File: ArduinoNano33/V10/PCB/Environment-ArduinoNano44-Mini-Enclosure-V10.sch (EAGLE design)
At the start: 53 parts, among them IC1 BME680, Q1 310mA/60V/1.6Ω, Q2 310mA/60V/1.6Ω

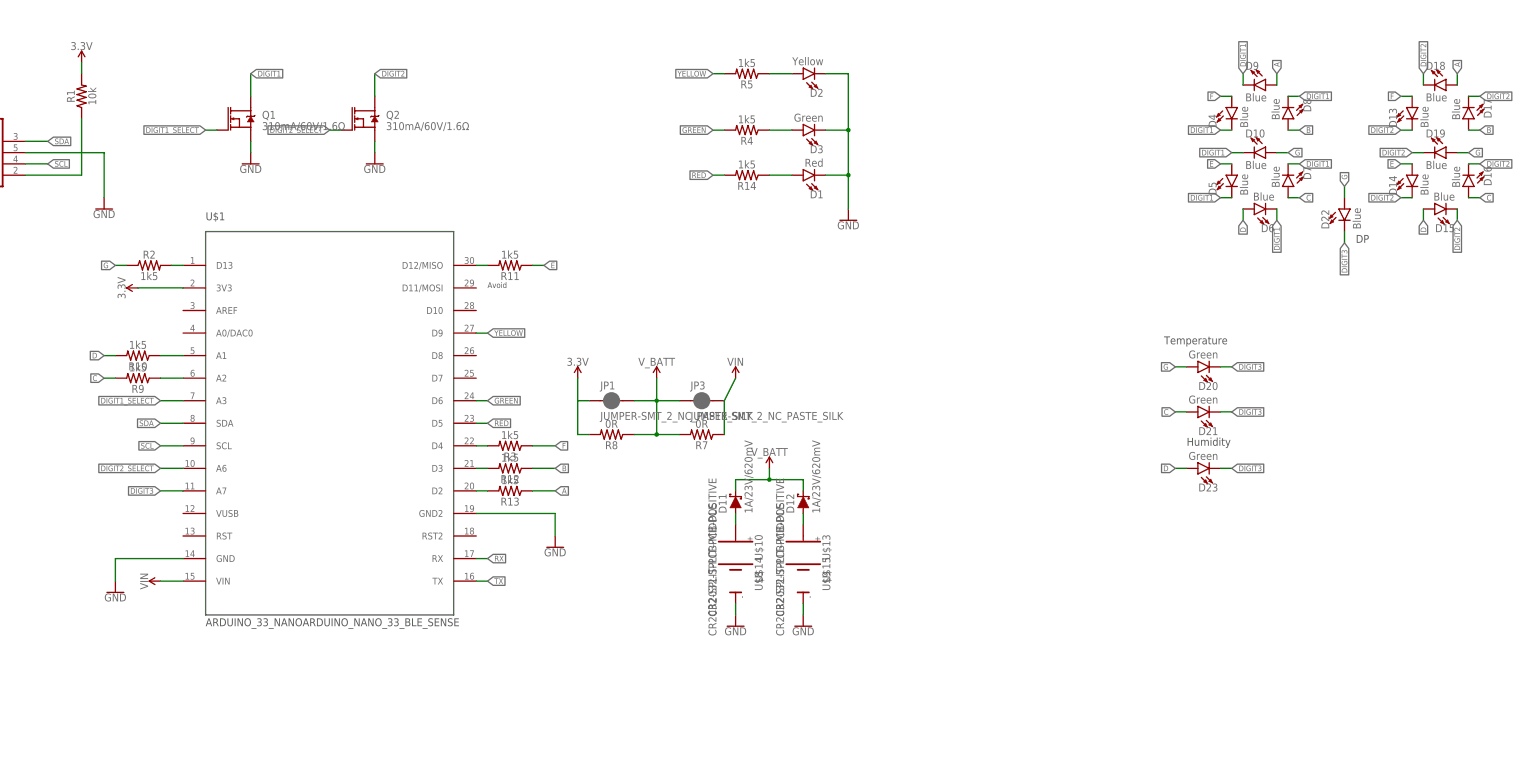
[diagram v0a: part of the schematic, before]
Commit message: added 7 segment display from LEDs.
Added batteries as internal layers
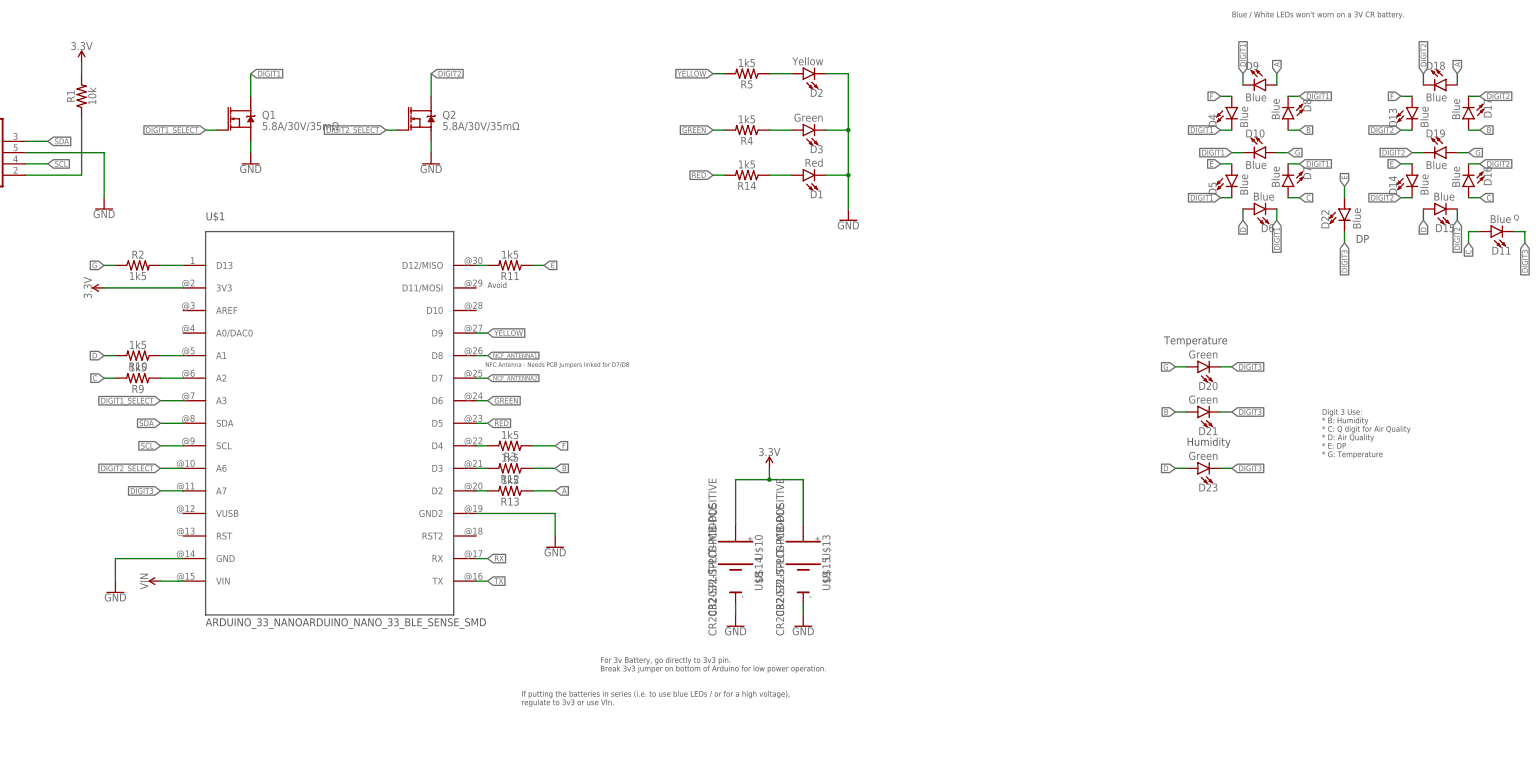
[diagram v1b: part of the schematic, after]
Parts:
- removed D12: 1A/23V/620mV, SparkFun-DiscreteSemi:DIODE-SCHOTTKY-BAT20J
- removed JP1, JP3: JUMPER-SMT_2_NC_PASTE_SILK, SparkFun-Jumpers:JUMPER-SMT_2_NC_PASTE_SILK
- removed R7, R8: 0R, SparkFun-Resistors:RESISTOR0805
- D11: value 1A/23V/620mV -> Blue; device SparkFun-DiscreteSemi:DIODE-SCHOTTKY-BAT20J -> ThingySticks:LED1206
- Q1, Q2: value 310mA/60V/1.6Ω -> 5.8A/30V/35mΩ; device SparkFun-DiscreteSemi:MOSFET-NCH-2N7002PW -> SparkFun-DiscreteSemi:MOSFET-NCH-AO3404A
- U$1: value ARDUINO_33_NANOARDUINO_NANO_33_BLE_SENSE -> ARDUINO_33_NANOARDUINO_NANO_33_BLE_SENSE_SMD; device ThingySticks:ARDUINO_33_NANOARDUINO_NANO_33_BLE_SENSE -> ThingySticks:ARDUINO_33_NANOARDUINO_NANO_33_BLE_SENSE_SMD
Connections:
- removed net N$5: D11.A, U$10.+
- removed net N$6: D12.A, U$13.+
- removed net V_BATT: D11.C, D12.C, JP1.2, JP3.1, R7.2, R8.1
- new net NCF_ANTENNA1: U$1.D8
- new net NCF_ANTENNA2: U$1.D7
- net 3.3V: now also U$10.+, U$13.+; no longer JP1.1, R8.2
- net B: now also D21.A
- net C: now also D11.A; no longer D21.A
- net DIGIT3: now also D11.C
- net E: now also D22.A
- net G: no longer D22.A
- net VIN: no longer JP3.2, R7.1
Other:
- note added: "Blue / White LEDs won't worn on a 3V CR battery."
- note added: "Digit 3 Use: * B: Humidity * C: Q digit for Air Quality * D: Air Quality * E: DP * G: Temperature"
- note added: "For 3v Battery, go directly to 3v3 pin. Break 3v3 jumper on bottom of Arduino for low power operation."
- note added: "If putting the batteries in series (i.e. to use blue LEDs / or for a high voltage), regulate to 3v3 or use VIn."
- note added: "NFC Antenna - Needs PCB Jumpers linked for D7/D8"
- note added: "Q"
- moved on the sheet: Q2, R2

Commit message: Split out personal environmental sensor boards into individual Eagle files.
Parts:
- removed JP2: USB-NEW-MICROB, Tinamous:USB-NEW-MICROB
- added J1, J10, J3, J6, J7, J8, J9: (no value), SparkFun-Connectors:CONN_01
- added J4: QUIC, SparkFun-Connectors-2020-01-17:CONN_04SMD2
- added J5: (no value), SparkFun-Connectors-2020-01-17:USB_C2-LAYER
- added LOGO2, LOGO3: OSHW-LOGOL, SparkFun-Aesthetics:OSHW-LOGOL
- added LOGO7: OSHW-LOGOM, SparkFun-Aesthetics:OSHW-LOGOM
- added R6, R7: 5k1, SparkFun-Resistors:RESISTOR0805
- added S1: MOMENTARY-SWITCH-SPST-SMD-5.2MM, ThingySticks:MOMENTARY-SWITCH-SPST-SMD-5.2MM
- added TOGGLE1: MOMENTARY-SWITCH-SPST-SMD-6.0X3.5MM, ThingySticks:MOMENTARY-SWITCH-SPST-SMD-6.0X3.5MM
- added U$11, U$12, U$16, U$17, U$18, U$19, U$20, U$7: CR2032-SPLIT-PCB-POSITIVE, ThingySticks:CR2032-SPLIT-PCB-POSITIVE
- added U$2, U$3, U$6: (no value), ThingySticks:CR2032SMT
- J2: device SparkFun-Connectors:CONN_03SMD -> SparkFun-Connectors:CONN_01
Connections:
- new net A0: J2.1, S1.1, TOGGLE1.1, U$1.A0/DAC0
- new net CC1: J5.CC1, R7.1
- new net CC2: J5.CC2, R6.1
- new net D+: J5.D+
- new net D-: J5.D-
- new net N$43: J3.1, U$1.D11/MOSI
- new net SHIELD: J5.SHLD
- new net SWITCH1: U$1.D10
- net 3.3V: now also J4.2, U$11.+, U$12.+, U$16.+, U$17.+, U$18.+, U$19.+, U$2.+, U$2.+1, U$20.+, U$3.+, U$3.+1, U$6.+1, U$7.+
- net GND: now also J4.1, J5.GND, R6.2, R7.2, S1.2, TOGGLE1.2, U$2.-, U$3.-, U$6.-; no longer J2.1, JP2.GND
- net NCF_ANTENNA1: now also J6.1
- net NCF_ANTENNA2: now also J1.1
- net SCL: now also J4.4
- net SDA: now also J4.3
- net VIN: now also J5.VBUS; no longer J2.3, JP2.D+
